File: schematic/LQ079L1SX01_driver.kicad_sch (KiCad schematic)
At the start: 138 parts, among them J1 690-019-298-412, J2 Header, Q1 1AM, Q12 1AM, Q4 1AM, Q4 2A, Q5 S1, Q6 S1, Q7 1AM, Q8 B07JP, U2 LT6911C, U3 Unknown_buck, U4 Unknown_buck, U5 Unknown_buck, U7 Unknown_boost, Y1 27MHz, 100ppm

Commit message: Update schematic
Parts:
- removed J2: Header, CM5IO:Hirose_FH12-22S-0.5SH_1x22-1MP_P0.50mm_Horizontal, symbol Connector:Conn_01x22_Socket
- added CI1, CI2, CI3, CI4, CI5: 1u, Capacitor_SMD:C_0805_2012Metric_Pad1.18x1.45mm_HandSolder, symbol Device:C
- added J2, J4: Conn_01x60_Socket, symbol Connector:Conn_01x60_Socket
- added JI2: Conn_02x25_Odd_Even, symbol Connector_Generic:Conn_02x25_Odd_Even
- added RI1, RI2: R, symbol Device:R
- added U1: LP3102, Package_DFN_QFN:TDFN-10-1EP_2x3mm_P0.5mm_EP0.9x2mm, symbol Regulator_Switching:MAX17501AxTB
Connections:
- net 5V_fused: now also J2.32 (Pin_32), J2.35 (Pin_35), J2.38 (Pin_38), J2.40 (Pin_40)
- net GND: now also CI1.2, CI2.2, RI2.1, U1.11 (GND)
- net at C76.2, Q4.2 (S), Q6.2 (S)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: now also J2.41 (Pin_41), J2.42 (Pin_42)
- net at C77.2, Q5.2 (S), R38.1: now also J2.33 (Pin_33), J2.34 (Pin_34)
- net at C46.1, D8.1 (K), R28.2: now also J2.51 (Pin_51), J2.52 (Pin_52), J2.53 (Pin_53)
- net at R31.2, R35.2, U7.3 (????): now also J2.55 (Pin_55), J2.56 (Pin_56), J2.57 (Pin_57), J2.58 (Pin_58), J2.59 (Pin_59), J2.60 (Pin_60)
- net at C69.1, C70.1, C71.1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: now also J2.36 (Pin_36), J2.37 (Pin_37)
- net at U2.35 (M0_L3_P3): now also J2.30 (Pin_30)
- net at U2.36 (M0_L3_N3): now also J2.29 (Pin_29)
- net at U2.37 (M1_LCK_P3): now also J2.27 (Pin_27)
- net at U2.38 (M1_LCK_N3): now also J2.26 (Pin_26)
- net at U2.39 (MCK_L2_P3): now also J2.24 (Pin_24)
- net at U2.40 (MCK_L2_N3): now also J2.23 (Pin_23)
- net at U2.41 (M2_L1_P3): now also J2.21 (Pin_21)
- net at U2.42 (M2_L1_N3): now also J2.20 (Pin_20)
- net at U2.43 (M2_L0_P3): now also J2.18 (Pin_18)
- net at U2.44 (M2_L0_N3): now also J2.17 (Pin_17)
- net at U2.49 (M0_L3_P1): now also J2.15 (Pin_15)
- net at U2.50 (M0_L3_N1): now also J2.14 (Pin_14)
- net at U2.51 (M0_LCK_P1): now also J2.12 (Pin_12)
- net at U2.52 (M0_LCK_N1): now also J2.11 (Pin_11)
- net at U2.53 (MCK_L2_P1): now also J2.9 (Pin_9)
- net at U2.54 (MCK_L2_N1): now also J2.8 (Pin_8)
- net at U2.55 (M2_L1_P1): now also J2.6 (Pin_6)
- net at U2.56 (M2_L1_N1): now also J2.5 (Pin_5)
- net at U2.57 (M3_L0_P1): now also J2.3 (Pin_3)
- net at U2.58 (M3_L0_N1): now also J2.2 (Pin_2)
- net 2V renamed 1.8V
- net 1.8V: now also J2.39 (Pin_39)
- new net: CI5.1, U1.1 (C3P)
- new net: CI5.2, U1.10 (C3N)
- new net: J2.1 (Pin_1), J2.10 (Pin_10), J2.13 (Pin_13), J2.16 (Pin_16), J2.19 (Pin_19), J2.22 (Pin_22), J2.25 (Pin_25), J2.28 (Pin_28), J2.31 (Pin_31), J2.4 (Pin_4), J2.44 (Pin_44), J2.46 (Pin_46), J2.49 (Pin_49), J2.7 (Pin_7)
- new net: J4.1 (Pin_1), J4.2 (Pin_2), J4.3 (Pin_3), J4.4 (Pin_4), J4.5 (Pin_5), J4.6 (Pin_6), JI2.1 (Pin_1), JI2.3 (Pin_3), JI2.5 (Pin_5), JI2.7 (Pin_7)
- new net: J4.32 (Pin_32), JI2.10 (Pin_10)
- new net: J4.10 (Pin_10), J4.8 (Pin_8), J4.9 (Pin_9), JI2.11 (Pin_11), JI2.13 (Pin_13)
- new net: J4.31 (Pin_31), JI2.12 (Pin_12)
- new net: JI2.14 (Pin_14), JI2.2 (Pin_2), JI2.20 (Pin_20), JI2.26 (Pin_26), JI2.29 (Pin_29), JI2.32 (Pin_32), JI2.38 (Pin_38), JI2.39 (Pin_39), JI2.44 (Pin_44), JI2.45 (Pin_45), JI2.50 (Pin_50), JI2.8 (Pin_8)
- new net: J4.38 (Pin_38), JI2.16 (Pin_16)
- new net: J4.22 (Pin_22), JI2.17 (Pin_17)
- new net: J4.37 (Pin_37), JI2.18 (Pin_18)
- new net: CI1.1, JI2.19 (Pin_19), JI2.21 (Pin_21), U1.9 (VP)
- new net: J4.35 (Pin_35), JI2.22 (Pin_22)
- new net: J4.34 (Pin_34), JI2.24 (Pin_24)
- new net: JI2.25 (Pin_25), JI2.27 (Pin_27), U1.2 (VN)
- new net: J4.41 (Pin_41), JI2.28 (Pin_28)
- new net: J4.40 (Pin_40), JI2.30 (Pin_30)
- new net: J4.19 (Pin_19), J4.20 (Pin_20), JI2.31 (Pin_31)
- new net: J4.59 (Pin_59), JI2.34 (Pin_34)
- new net: J4.58 (Pin_58), JI2.36 (Pin_36)
- new net: J4.44 (Pin_44), JI2.4 (Pin_4)
- new net: J4.46 (Pin_46), JI2.40 (Pin_40)
- new net: J4.55 (Pin_55), JI2.41 (Pin_41)
- new net: J4.47 (Pin_47), JI2.42 (Pin_42)
- new net: J4.56 (Pin_56), JI2.43 (Pin_43)
- new net: J4.52 (Pin_52), JI2.46 (Pin_46)
- new net: J4.49 (Pin_49), JI2.47 (Pin_47)
- new net: J4.53 (Pin_53), JI2.48 (Pin_48)
- new net: J4.50 (Pin_50), JI2.49 (Pin_49)
- new net: J4.43 (Pin_43), JI2.6 (Pin_6)
- new net: CI2.1, J4.24 (Pin_24), J4.25 (Pin_25), RI1.2, U1.6 (VIN)
- new net: CI3.1, U1.4 (C1N)
- new net: CI3.2, U1.3 (C1P)
- new net: RI1.1, RI2.2, U1.5 (EN)
- new net: J4.12 (Pin_12), J4.15 (Pin_15), J4.17 (Pin_17), J4.30 (Pin_30), J4.33 (Pin_33), J4.36 (Pin_36), J4.39 (Pin_39), J4.42 (Pin_42), J4.45 (Pin_45), J4.48 (Pin_48), J4.51 (Pin_51), J4.54 (Pin_54), J4.57 (Pin_57), J4.60 (Pin_60)
- new net: CI4.1, U1.8 (C2P)
- new net: CI4.2, U1.7 (C2N)
- no-connect marks 9 -> 27
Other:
- note added: "1.8V"
- note removed: "2V"
- moved on the sheet: C1, C12, C13, C14, C15, C16, C17, C18, C19, C2, C20, C21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

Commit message: Update schematic
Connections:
- net LED -: now reaches J4.1 (Pin_1), J4.2 (Pin_2), J4.3 (Pin_3), J4.4 (Pin_4), J4.5 (Pin_5), J4.6 (Pin_6), JI2.1 (Pin_1), JI2.3 (Pin_3), JI2.5 (Pin_5), JI2.7 (Pin_7)
- net LED+: now reaches J4.10 (Pin_10), J4.8 (Pin_8), J4.9 (Pin_9), JI2.11 (Pin_11), JI2.13 (Pin_13)
- net IOVCC: now reaches J4.22 (Pin_22), JI2.17 (Pin_17)
- net VSP: now reaches CI1.1, JI2.19 (Pin_19), JI2.21 (Pin_21), U1.9 (VP)
- net VSN: now reaches JI2.25 (Pin_25), JI2.27 (Pin_27), U1.2 (VN)
- net RESET: now reaches J4.19 (Pin_19), J4.20 (Pin_20), JI2.31 (Pin_31)
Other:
- note added: "LCD reset signal"
- note removed: "This should be LCD reset signal"
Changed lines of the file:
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@@
 	(wire
 		(pts
-			(xy 652.78 62.23) (xy 615.95 62.23)
-		)
-		(stroke
-			(width 0)
-			(type default)
-		)
-	)
-	(wire
-		(pts
 			(xy 552.45 311.15) (xy 552.45 313.69)
 		)
@@
 	(wire
 		(pts
+			(xy 636.27 80.01) (xy 652.78 80.01)
+		)
+		(stroke
+			(width 0)
+			(type default)
+		)
+	)
+	(wire
+		(pts
 			(xy 105.41 172.72) (xy 105.41 173.99)
 		)
@@
 	(wire
 		(pts
-			(xy 652.78 86.36) (xy 638.81 86.36)
-		)
-		(stroke
-			(width 0)
-			(type default)
-		)
-	)
-	(wire
-		(pts
 			(xy 138.43 469.9) (xy 138.43 472.44)
 		)
@@
 	(wire
 		(pts
+			(xy 591.82 41.91) (xy 652.78 41.91)
+		)
+		(stroke
+			(width 0)
+			(type default)
+		)
+	)
+	(wire
+		(pts
 			(xy 427.99 154.94) (xy 472.44 154.94)
 		)
@@
 	(wire
 		(pts
+			(xy 638.81 86.36) (xy 652.78 86.36)
+		)
+		(stroke
+			(width 0)
+			(type default)
+		)
+	)
+	(wire
+		(pts
 			(xy 381 135.89) (xy 388.62 135.89)
 		)
@@
 	(wire
 		(pts
+			(xy 603.25 46.99) (xy 652.78 46.99)
+		)
+		(stroke
+			(width 0)
+			(type default)
+		)
+	)
+	(wire
+		(pts
 			(xy 331.47 142.24) (xy 331.47 137.16)
 		)
@@
 	(wire
 		(pts
-			(xy 652.78 80.01) (xy 636.27 80.01)
-		)
-		(stroke
-			(width 0)
-			(type default)
-		)
-	)
-	(wire
-		(pts
 			(xy 224.79 411.48) (xy 234.95 411.48)
 		)
@@
 	(wire
 		(pts
-			(xy 652.78 41.91) (xy 591.82 41.91)
-		)
-		(stroke
-			(width 0)
-			(type default)
-		)
-	)
-	(wire
-		(pts
 			(xy 113.03 175.26) (xy 254 175.26)
 		)
@@
 	(wire
 		(pts
+			(xy 615.95 62.23) (xy 652.78 62.23)
+		)
+		(stroke
+			(width 0)
+			(type default)
+		)
+	)
+	(wire
+		(pts
 			(xy 337.82 203.2) (xy 337.82 204.47)
 		)
@@
 	(wire
 		(pts
-			(xy 652.78 46.99) (xy 603.25 46.99)
-		)
-		(stroke
-			(width 0)
-			(type default)
-		)
-	)
-	(wire
-		(pts
 			(xy 427.99 102.87) (xy 427.99 139.7)
 		)
@@
 		)
 	)
-	(text "This should be LCD reset signal"
+	(text "LCD reset signal"
 		(exclude_from_sim no)
 		(at 309.626 276.352 0)
@@
 		)
 	)
+	(label "VSP"
+		(at 648.97 76.2 180)
+		(fields_autoplaced yes)
+		(effects
+			(font
+				(size 1.27 1.27)
+			)
+			(justify right bottom)
+		)
+	)
+	(label "LED+"
+		(at 648.97 86.36 180)
+		(fields_autoplaced yes)
+		(effects
+			(font
+				(size 1.27 1.27)
+			)
+			(justify right bottom)
+		)
+	)
+	(label "LED -"
+		(at 650.24 96.52 180)
+		(fields_autoplaced yes)
+		(effects
+			(font
+				(size 1.27 1.27)
+			)
+			(justify right bottom)
+		)
+	)
 	(label "DSCL"
 		(at 92.71 176.53 0)
@@
 		)
 	)
+	(label "IOVCC"
+		(at 648.97 80.01 180)
+		(fields_autoplaced yes)
+		(effects
+			(font
+				(size 1.27 1.27)
+			)
+			(justify right bottom)
+		)
+	)
 	(label "RX_HPD"
 		(at 115.57 109.22 180)
@@
 		)
 	)
+	(label "RESET"
+		(at 648.97 62.23 180)
+		(fields_autoplaced yes)
+		(effects
+			(font
+				(size 1.27 1.27)
+			)
+			(justify right bottom)
+		)
+	)
 	(label "EN signal from STC"
 		(at 97.79 431.8 180)
 		(fields_autoplaced yes)
 		(effects
+			(font
+				(size 1.27 1.27)
+			)
+			(justify right bottom)
+		)
+	)
+	(label "VSN"
+		(at 648.97 68.58 180)
+		(fields_autoplaced yes)
+		(effects

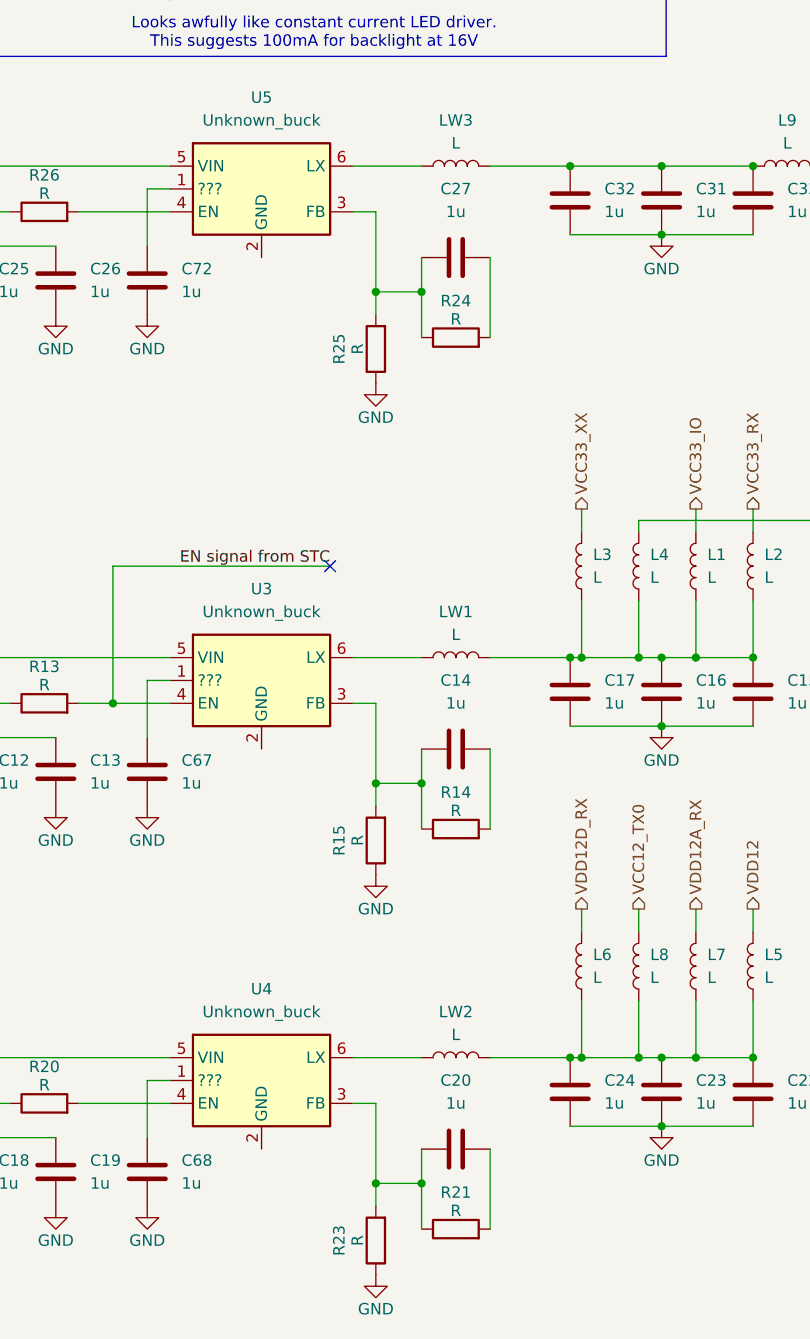
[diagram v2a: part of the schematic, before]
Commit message: Fix buck FB
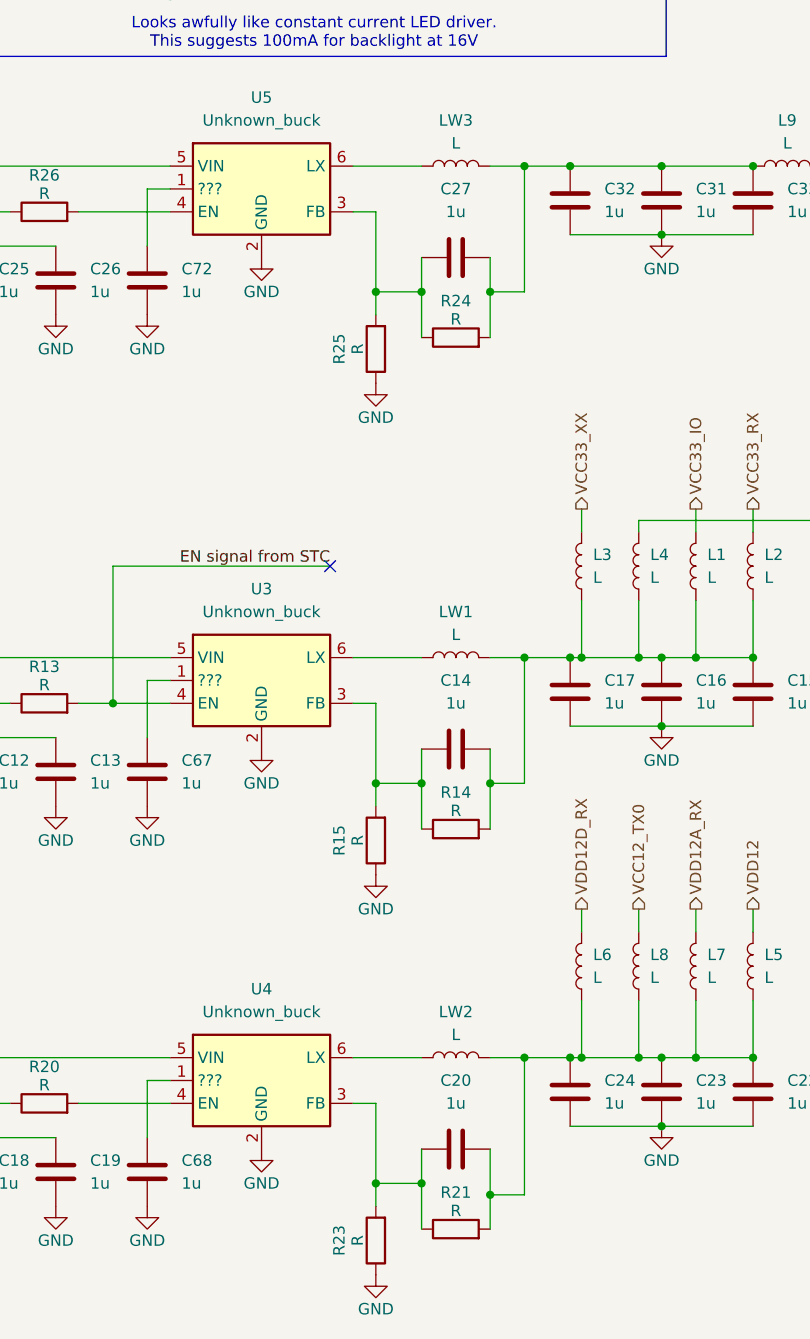
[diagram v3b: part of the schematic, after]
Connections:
- net GND: now also U3.2 (GND), U4.2 (GND), U5.2 (GND)
- net at C27.2, R24.2: now also C31.1, C32.1, C33.1, L9.1, LW3.2
- net at C15.1, C16.1, C17.1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: now also C14.2, R14.2
- net at C22.1, C23.1, C24.1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: now also C20.2, R21.2
